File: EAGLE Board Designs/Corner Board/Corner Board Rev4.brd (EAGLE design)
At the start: 64.8 x 44.5 mm, 64 parts, among them J1 CONNECTOR-8_AMPHENOL_M12A_08P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, J2 CONNECTOR-2_MICROFIT_SMD_RIGH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, J3 BINDER-M12-A_4_PIN, J4 CONNECTOR-4_μF_S_RA_, T1 78613/3C_78613/3C_AIRGAP, U1 LTC1563, U10 LTC6820, U11 MCP3204, U2 OPAMP_1_CHANNEL_OPA991, U3 INA823DT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

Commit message: Corner Board Finish
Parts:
- removed R21: RESISTOR_0603_2K, HyTechDevices:0603-RES
- moved R15 0.25 mm to (37.1, 25.9)
- moved R16 0.25 mm to (34.0, 25.9)
- moved R22 0.25 mm to (56.5, 29.5)
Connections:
- net +3V3: no longer R21.2
- net ADC_SDO: no longer R21.1
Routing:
- net ADC_SDO: track 19.8 -> 15.4 mm
- net +3V3: track 89.7 -> 87.8 mm

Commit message: dale papa
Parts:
- removed U$5: (no value), HyTechManufacturing:LOGO_HYTECH_MEDIUM
- C21: value CAPACITOR_0603_50V_10NF -> CAPACITOR_0603_35V_1UF
- C22: value CAPACITOR_0603_50V_10NF -> CAPACITOR_0603_35V_0.47UF
- R11: value RESISTOR_0603_13K -> RESISTOR_0603_12K
- R12: value RESISTOR_0603_75K -> RESISTOR_0603_7.5K
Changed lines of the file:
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@@
 <element name="U$4" library="HyTechManufacturing" package="LOGO_HYTECH_SMALL" value="" x="19.05" y="21.082" smashed="yes" rot="MR0"/>
 <element name="U$6" library="HyTechManufacturing" package="LOGO_GT_SMALL" value="" x="26.67" y="29.972" smashed="yes"/>
-<element name="U$5" library="HyTechManufacturing" package="LOGO_HYTECH_MEDIUM" value="" x="103.124" y="38.608" smashed="yes" rot="MR0"/>
 <element name="C12" library="HyTechDevices" package="0603-CAP" value="CAPACITOR_0603_10V_0.1UF" x="40.894" y="32.004" smashed="yes" rot="MR180">
 <attribute name="CAPACITANCE" value="0.1µF" x="40.894" y="32.004" size="1.778" layer="28" rot="MR180" display="off"/>
@@
 <element name="U$2" library="HyTechManufacturing" package="MOUNTING_M3" value="" x="60.96" y="3.81" smashed="yes"/>
 <element name="U$3" library="HyTechManufacturing" package="MOUNTING_M3" value="" x="60.96" y="40.64" smashed="yes"/>
-<element name="R11" library="HyTechDevices" package="0603-RES" value="RESISTOR_0603_13K" x="55.88" y="34.163" smashed="yes" rot="MR90">
-<attribute name="DKPN" value="P13KBECT-ND" x="55.88" y="34.163" size="1.778" layer="28" rot="MR90" display="off"/>
-<attribute name="MANUFACTURER" value="Panasonic Electronic Components" x="55.88" y="34.163" size="1.778" layer="28" rot="MR90" display="off"/>
-<attribute name="MOPN" value="667-ERA-3ARW133V" x="55.88" y="34.163" size="1.778" layer="28" rot="MR90" display="off"/>
-<attribute name="MPN" value="ERA-3ARW133V" x="55.88" y="34.163" size="1.778" layer="28" rot="MR90" display="off"/>
+<element name="R11" library="HyTechDevices" package="0603-RES" value="RESISTOR_0603_12K" x="55.88" y="34.163" smashed="yes" rot="MR90">
+<attribute name="DKPN" value="311-12.0KHRCT-ND" x="55.88" y="34.163" size="1.778" layer="28" rot="MR90" display="off"/>
+<attribute name="MANUFACTURER" value="Yageo" x="55.88" y="34.163" size="1.778" layer="28" rot="MR90" display="off"/>
+<attribute name="MOPN" value="603-RC0603FR-0712KL" x="55.88" y="34.163" size="1.778" layer="28" rot="MR90" display="off"/>
+<attribute name="MPN" value="RC0603FR-0712KL" x="55.88" y="34.163" size="1.778" layer="28" rot="MR90" display="off"/>
 <attribute name="NAME" x="56.769" y="34.417" size="0.8128" layer="26" font="vector" rot="MR90" align="bottom-center"/>
 <attribute name="POWER" value="0.1W" x="55.88" y="34.163" size="1.778" layer="28" rot="MR90" display="off"/>
-<attribute name="RESISTANCE" value="13k" x="55.88" y="34.163" size="1.778" layer="28" rot="MR90" display="off"/>
-<attribute name="TOLERANCE" value="0.05%" x="55.88" y="34.163" size="1.778" layer="28" rot="MR90" display="off"/>
-<attribute name="VOLTAGE_CONTINUOUS" value="75V" x="55.88" y="34.163" size="1.778" layer="28" rot="MR90" display="off"/>
-<attribute name="VOLTAGE_MAX" value="150V" x="55.88" y="34.163" size="1.778" layer="28" rot="MR90" display="off"/>
+<attribute name="RESISTANCE" value="12k" x="55.88" y="34.163" size="1.778" layer="28" rot="MR90" display="off"/>
+<attribute name="TOLERANCE" value="1%" x="55.88" y="34.163" size="1.778" layer="28" rot="MR90" display="off"/>
+<attribute name="VOLTAGE_CONTINUOUS" value="34.64V" x="55.88" y="34.163" size="1.778" layer="28" rot="MR90" display="off"/>
+<attribute name="VOLTAGE_MAX" value="75V" x="55.88" y="34.163" size="1.778" layer="28" rot="MR90" display="off"/>
 </element>
-<element name="R12" library="HyTechDevices" package="0603-RES" value="RESISTOR_0603_75K" x="52.578" y="29.21" smashed="yes" rot="MR270">
-<attribute name="DKPN" value="RT0603BRE0775KL-ND" x="52.578" y="29.21" size="1.778" layer="28" rot="MR270" display="off"/>
-<attribute name="MANUFACTURER" value="Yageo" x="52.578" y="29.21" size="1.778" layer="28" rot="MR270" display="off"/>
-<attribute name="MOPN" value="603-RT0603BRE0775KL" x="52.578" y="29.21" size="1.778" layer="28" rot="MR270" display="off"/>
-<attribute name="MPN" value="RT0603BRE0775KL" x="52.578" y="29.21" size="1.778" layer="28" rot="MR270" display="off"/>
+<element name="R12" library="HyTechDevices" package="0603-RES" value="RESISTOR_0603_7.5K" x="52.578" y="29.21" smashed="yes" rot="MR270">
+<attribute name="DKPN" value="P20072CT-ND" x="52.578" y="29.21" size="1.778" layer="28" rot="MR270" display="off"/>
+<attribute name="MANUFACTURER" value="Panasonic Electronic Components" x="52.578" y="29.21" size="1.778" layer="28" rot="MR270" display="off"/>
+<attribute name="MOPN" value="667-ERJ-PB3B7501V" x="52.578" y="29.21" size="1.778" layer="28" rot="MR270" display="off"/>
+<attribute name="MPN" value="ERJ-PB3B7501V" x="52.578" y="29.21" size="1.778" layer="28" rot="MR270" display="off"/>
 <attribute name="NAME" x="51.689" y="29.21" size="0.8128" layer="26" font="vector" rot="MR270" align="bottom-center"/>
-<attribute name="POWER" value="0.1W" x="52.578" y="29.21" size="1.778" layer="28" rot="MR270" display="off"/>
-<attribute name="RESISTANCE" value="75k" x="52.578" y="29.21" size="1.778" layer="28" rot="MR270" display="off"/>
+<attribute name="POWER" value="0.2W" x="52.578" y="29.21" size="1.778" layer="28" rot="MR270" display="off"/>
+<attribute name="RESISTANCE" value="7.5k" x="52.578" y="29.21" size="1.778" layer="28" rot="MR270" display="off"/>
 <attribute name="TOLERANCE" value="0.1%" x="52.578" y="29.21" size="1.778" layer="28" rot="MR270" display="off"/>
-<attribute name="VOLTAGE_CONTINUOUS" value="75V" x="52.578" y="29.21" size="1.778" layer="28" rot="MR270" display="off"/>
-<attribute name="VOLTAGE_MAX" value="75V" x="52.578" y="29.21" size="1.778" layer="28" rot="MR270" display="off"/>
+<attribute name="VOLTAGE_CONTINUOUS" value="38.73V" x="52.578" y="29.21" size="1.778" layer="28" rot="MR270" display="off"/>
+<attribute name="VOLTAGE_MAX" value="150V" x="52.578" y="29.21" size="1.778" layer="28" rot="MR270" display="off"/>
 </element>
-<element name="C21" library="HyTechDevices" package="0603-CAP" value="CAPACITOR_0603_50V_10NF" x="48.768" y="30.48" smashed="yes" rot="MR180">
-<attribute name="CAPACITANCE" value="10nF" x="48.768" y="30.48" size="1.778" layer="28" rot="MR180" display="off"/>
-<attribute name="DKPN" value="445-7404-1-ND" x="48.768" y="30.48" size="1.778" layer="28" rot="MR180" display="off"/>
+<element name="C21" library="HyTechDevices" package="0603-CAP" value="CAPACITOR_0603_35V_1UF" x="48.768" y="30.48" smashed="yes" rot="MR180">
+<attribute name="CAPACITANCE" value="1µF" x="48.768" y="30.48" size="1.778" layer="28" rot="MR180" display="off"/>
+<attribute name="DKPN" value="445-173625-1-ND" x="48.768" y="30.48" size="1.778" layer="28" rot="MR180" display="off"/>
 <attribute name="MANUFACTURER" value="TDK Corporation" x="48.768" y="30.48" size="1.778" layer="28" rot="MR180" display="off"/>
-<attribute name="MOPN" value="810-C1608C0G1H103J" x="48.768" y="30.48" size="1.778" layer="28" rot="MR180" display="off"/>
-<attribute name="MPN" value="C1608C0G1H103J080AA" x="48.768" y="30.48" size="1.778" layer="28" rot="MR180" display="off"/>
+<attribute name="MOPN" value="810-C1608X7R1V105KAE" x="48.768" y="30.48" size="1.778" layer="28" rot="MR180" display="off"/>
+<attribute name="MPN" value="C1608X7R1V105K080AE" x="48.768" y="30.48" size="1.778" layer="28" rot="MR180" display="off"/>
 <attribute name="NAME" x="48.768" y="29.476" size="0.8128" layer="26" font="vector" rot="MR180" align="bottom-center"/>
-<attribute name="TOLERANCE" value="5%" x="48.768" y="30.48" size="1.778" layer="28" rot="MR180" display="off"/>
-<attribute name="VOLTAGE" value="50V" x="48.768" y="30.48" size="1.778" layer="28" rot="MR180" display="off"/>
+<attribute name="TOLERANCE" value="10%" x="48.768" y="30.48" size="1.778" layer="28" rot="MR180" display="off"/>
+<attribute name="VOLTAGE" value="35V" x="48.768" y="30.48" size="1.778" layer="28" rot="MR180" display="off"/>
 </element>
-<element name="C22" library="HyTechDevices" package="0603-CAP" value="CAPACITOR_0603_50V_10NF" x="54.229" y="29.337" smashed="yes" rot="MR270">
-<attribute name="CAPACITANCE" value="10nF" x="54.229" y="29.337" size="1.778" layer="28" rot="MR270" display="off"/>
-<attribute name="DKPN" value="445-7404-1-ND" x="54.229" y="29.337" size="1.778" layer="28" rot="MR270" display="off"/>
+<element name="C22" library="HyTechDevices" package="0603-CAP" value="CAPACITOR_0603_35V_0.47UF" x="54.229" y="29.337" smashed="yes" rot="MR270">
+<attribute name="CAPACITANCE" value="0.47µF" x="54.229" y="29.337" size="1.778" layer="28" rot="MR270" display="off"/>
+<attribute name="DKPN" value="445-6928-6-ND" x="54.229" y="29.337" size="1.778" layer="28" rot="MR270" display="off"/>
 <attribute name="MANUFACTURER" value="TDK Corporation" x="54.229" y="29.337" size="1.778" layer="28" rot="MR270" display="off"/>
-<attribute name="MOPN" value="810-C1608C0G1H103J" x="54.229" y="29.337" size="1.778" layer="28" rot="MR270" display="off"/>
-<attribute name="MPN" value="C1608C0G1H103J080AA" x="54.229" y="29.337" size="1.778" layer="28" rot="MR270" display="off"/>
+<attribute name="MOPN" value="810-CGA3E1X7R1V474K" x="54.229" y="29.337" size="1.778" layer="28" rot="MR270" display="off"/>
+<attribute name="MPN" value="CGA3E1X7R1V474K080AC" x="54.229" y="29.337" size="1.778" layer="28" rot="MR270" display="off"/>
 <attribute name="NAME" x="54.229" y="28.079" size="0.8128" layer="26" font="vector" rot="MR180" align="bottom-center"/>
-<attribute name="TOLERANCE" value="5%" x="54.229" y="29.337" size="1.778" layer="28" rot="MR270" display="off"/>
-<attribute name="VOLTAGE" value="50V" x="54.229" y="29.337" size="1.778" layer="28" rot="MR270" display="off"/>
+<attribute name="TOLERANCE" value="10%" x="54.229" y="29.337" size="1.778" layer="28" rot="MR270" display="off"/>
+<attribute name="VOLTAGE" value="35V" x="54.229" y="29.337" size="1.778" layer="28" rot="MR270" display="off"/>
 </element>
 <element name="U4" library="HyTechDevices" package="SOT-23-8" value="OPAMP_2_CHANNEL_OPA_2991" x="52.832" y="32.512" smashed="yes" rot="MR270">

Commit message: woohoo filter added!!!!
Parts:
- removed C12: CAPACITOR_0603_10V_0.1UF, HyTechDevices:0603-CAP
- removed C8: CAPACITOR_0603_10V_1UF, HyTechDevices:0603-CAP
- removed R15, R16: RESISTOR_0603_4.22M, HyTechDevices:0603-RES
- removed U2: OPAMP_1_CHANNEL_OPA991, HyTechDevices:SC-70-5
- added C13, C14, C7: CAPACITOR_0603_10V_1UF, HyTechDevices:0603-CAP
- C6: value CAPACITOR_0603_10V_0.1UF -> CAPACITOR_0603_16V_0.47UF
- R14: value RESISTOR_0603_4.22M -> RESISTOR_0603_20K
- R3: value RESISTOR_0603_4.22M -> RESISTOR_0603_7.5K
- R6: value RESISTOR_0603_1K -> RESISTOR_0603_7.5K
- R7, R8: value RESISTOR_0603_4.22M -> RESISTOR_0603_12K
- U1: value LTC1563 -> OPAMP_2_CHANNEL_OPA_2991; device HyTechDevices:SSOP-16 -> HyTechDevices:SOT-23-8
- moved R6 11.3 mm to (37.2, 33.3), turned to 270 degrees
- moved R7 9.34 mm to (27.7, 32.3), turned to 270 degrees
- moved R3 9.09 mm to (30.1, 31.5), turned to 180 degrees
- moved R14 7.50 mm to (38.0, 29.2), turned to 0 degrees
- moved C1 5.86 mm to (34.0, 28.6), turned to 0 degrees
- moved C6 4.54 mm to (30.1, 33.0), turned to 180 degrees
- moved R1 3.95 mm to (29.3, 29.2)
- moved R2 2.96 mm to (30.9, 29.1)
- moved U1 2.41 mm to (34.0, 31.2), turned to 90 degrees
- moved R8 2.05 mm to (34.8, 33.8), turned to 180 degrees
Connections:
- removed net N$12: R15.2, U1.4
- removed net N$15: R7.1, U1.13
- removed net N$18: R14.2, R15.1, R16.1, U1.2
- removed net N$3: R6.1, U3.6
- new net LOAD_CELL_POST_INA: R7.1, U3.6
- net +3V3: now also U1.8; no longer C12.1, C8.1, U1.1, U1.16, U2.5
- net GND: now also C14.1, R14.1, U1.4; no longer C12.2, C8.2, U1.10, U1.12, U1.14, U1.3, U1.5, U1.8, U1.9, U2.2
- net LOAD_CELL_AMPLIFIED: now also C7.2, R8.1, U1.1; no longer R14.1, U2.4
- net LOAD_CELL_FILTERED: now also C13.2, R14.2, U1.6, U1.7; no longer R3.1, U1.15
- net N$1: now also U1.2; no longer U2.3
- net N$10: now also C14.2, R6.2, U1.5; no longer R3.2, R7.2, R8.1, U1.11
- net N$11: now also C7.1, R3.1, R7.2; no longer R16.2, R8.2, U1.6
- net N$6: now also C6.2, R3.2, U1.3; no longer R6.2, U2.1
- net N$8: now also C13.1, R6.1, R8.2; no longer C6.2, U1.7
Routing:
- net +3V3: track 87.8 -> 68.8 mm, vias 6 -> 5
- net N$18: track 11.5 -> 0.00 mm
- net LOAD_CELL_AMPLIFIED: track 2.98 -> 11.3 mm
- net N$11: track 10.4 -> 3.10 mm
- net LOAD_CELL_POST_INA: track 0.00 -> 4.21 mm
- net N$8: track 3.92 -> 8.13 mm
- net N$10: track 7.07 -> 3.64 mm
- net N$12: track 2.05 -> 0.00 mm
- net N$15: track 1.92 -> 0.00 mm
- net LOAD_CELL_FILTERED: track 15.0 -> 16.8 mm
- net N$3: track 1.73 -> 0.00 mm
- net N$6: track 1.74 -> 3.37 mm
- net N$1: track 3.29 -> 3.85 mm

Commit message: no drc errors
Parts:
- moved R2 0.13 mm to (30.9, 29.2)

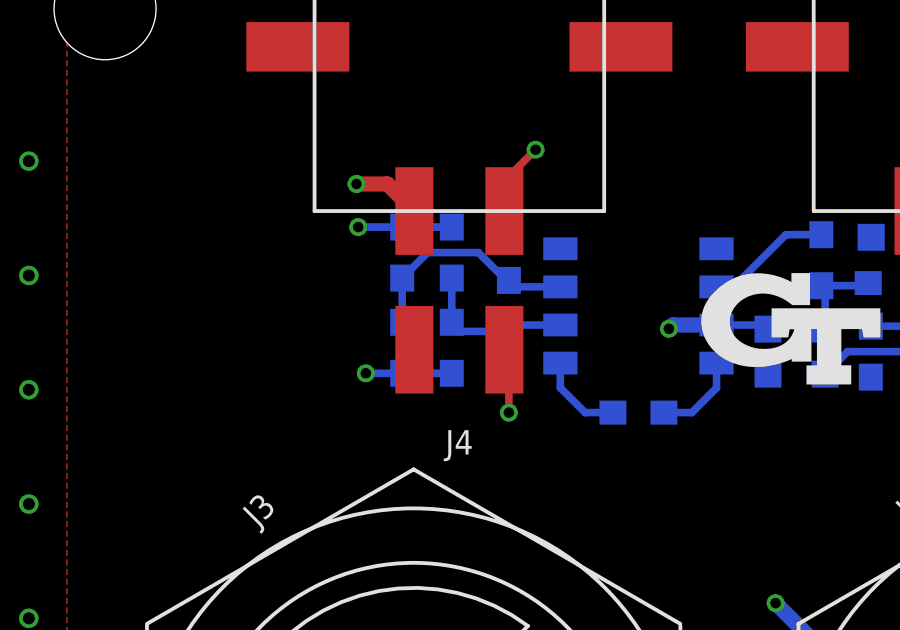
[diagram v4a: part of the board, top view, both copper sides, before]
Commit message: add descriptions and move via
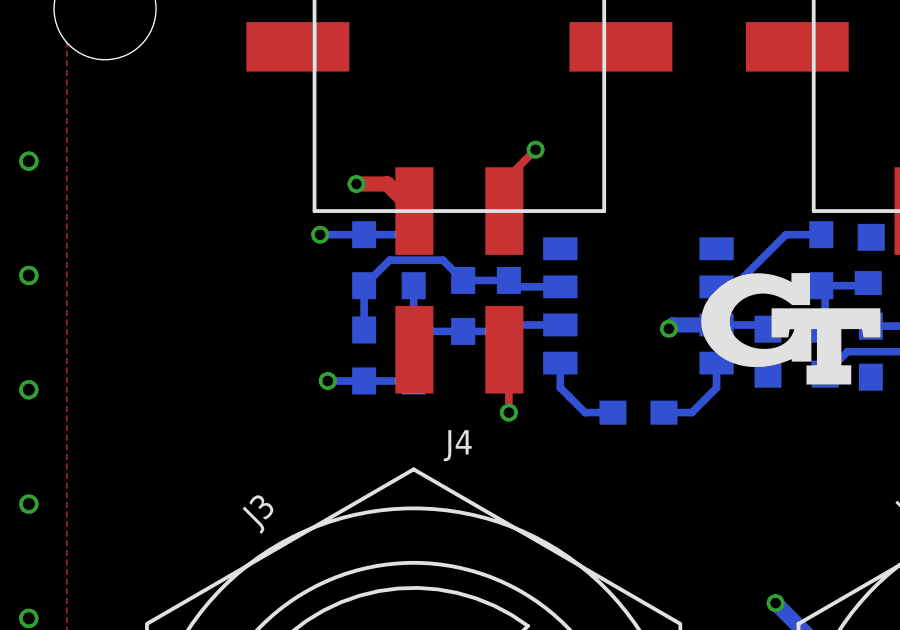
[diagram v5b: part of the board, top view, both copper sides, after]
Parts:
- added R15: RESISTOR_0603_DNP, HyTechDevices:0603-RES
- moved JP4 1.30 mm to (14.1, 29.1)
- moved JP3 1.30 mm to (14.1, 32.3)
- moved JP2 1.30 mm to (12.4, 29.1)
- moved JP1 1.30 mm to (12.4, 32.3)
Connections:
- net N$7: now also R15.1
- net N$9: now also R15.2
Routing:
- net SIGNAL_P: track 33.8 -> 32.4 mm
- net SIGNAL_N: track 33.7 -> 32.3 mm
- net N$7: track 5.31 -> 6.47 mm
- net N$9: track 7.61 -> 8.74 mm
